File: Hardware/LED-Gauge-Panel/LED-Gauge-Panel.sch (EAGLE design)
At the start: 3 parts

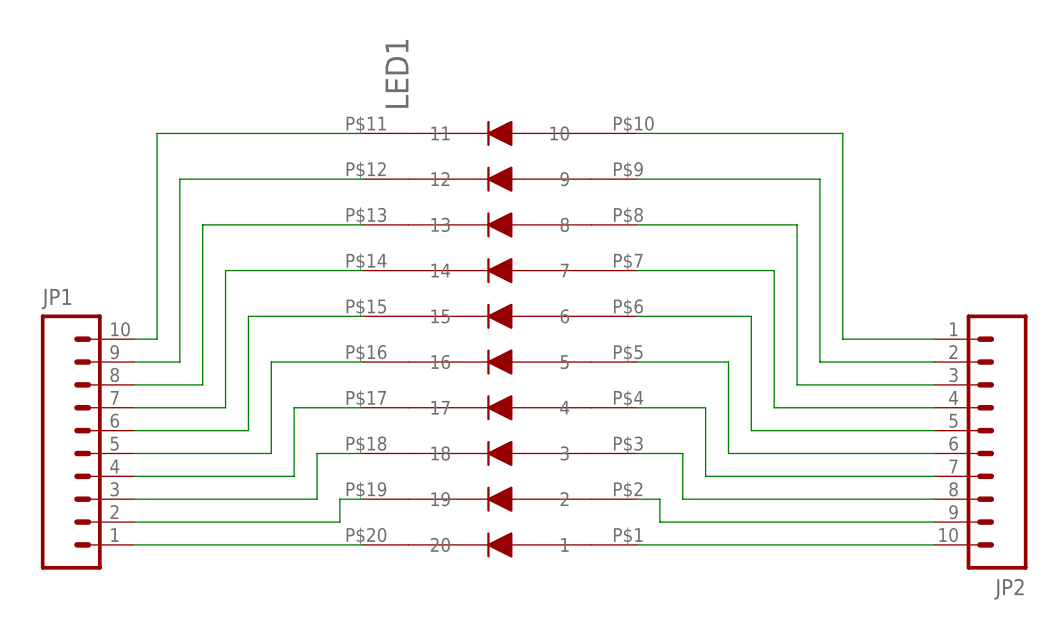
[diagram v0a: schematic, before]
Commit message: Create library part for LED display button, update PCB with LED button part
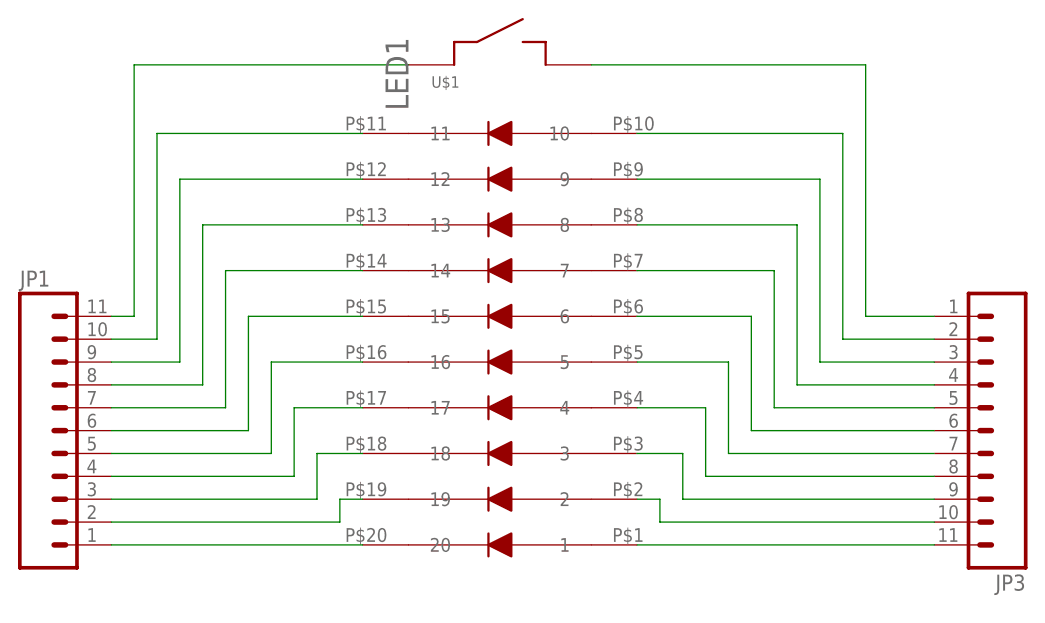
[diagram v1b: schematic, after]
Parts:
- removed JP2: (no value), SparkFun-Connectors:M10SILK_FEMALE_PTH
- added JP3: (no value), SparkFun-Connectors:M11PTH
- added U$1: MOMENTARY-SWITCH-EVQ1, 2016PowerPackLibraries:MOMENTARY-SWITCH-EVQ1
- JP1: device SparkFun-Connectors:M10SILK_FEMALE_PTH -> SparkFun-Connectors:M11PTH
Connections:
- new net N$21: JP1.11, U$1.P$1
- new net N$22: JP3.1, U$1.P$2
- net N$11: now also JP3.11; no longer JP2.10
- net N$12: now also JP3.10; no longer JP2.9
- net N$13: now also JP3.9; no longer JP2.8
- net N$14: now also JP3.8; no longer JP2.7
- net N$15: now also JP3.7; no longer JP2.6
- net N$16: now also JP3.6; no longer JP2.5
- net N$17: now also JP3.5; no longer JP2.4
- net N$18: now also JP3.4; no longer JP2.3
- net N$19: now also JP3.3; no longer JP2.2
- net N$20: now also JP3.2; no longer JP2.1
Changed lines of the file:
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@@
 <setting verticaltext="up"/>
 </settings>
-<grid distance="0.1" unitdist="inch" unit="inch" style="lines" multiple="1" display="yes" altdistance="0.01" altunitdist="inch" altunit="inch"/>
+<grid distance="0.1" unitdist="inch" unit="inch" style="lines" multiple="1" display="no" altdistance="0.01" altunitdist="inch" altunit="inch"/>
 <layers>
 <layer number="1" name="Top" color="4" fill="1" visible="no" active="no"/>
@@
 </classes>
 <parts>
-<part name="JP1" library="SparkFun-Connectors" deviceset="M10" device="SILK_FEMALE_PTH"/>
-<part name="JP2" library="SparkFun-Connectors" deviceset="M10" device="SILK_FEMALE_PTH"/>
+<part name="JP1" library="SparkFun-Connectors" deviceset="M11" device="PTH"/>
 <part name="LED1" library="2016PowerPackLibraries" deviceset="LED-DC7G3HWA" device=""/>
+<part name="U$1" library="2016PowerPackLibraries" deviceset="MOMENTARY-SWITCH-EVQ1" device=""/>
+<part name="JP3" library="SparkFun-Connectors" deviceset="M11" device="PTH"/>
 </parts>
 <sheets>
@@
 </plain>
 <instances>
-<instance part="JP1" gate="G$1" x="0" y="20.32"/>
-<instance part="JP2" gate="G$1" x="109.22" y="7.62" rot="R180"/>
+<instance part="JP1" gate="G$1" x="-2.54" y="15.24"/>
 <instance part="LED1" gate="G$1" x="55.88" y="2.54" rot="R90"/>
+<instance part="U$1" gate="G$1" x="45.72" y="55.88"/>
+<instance part="JP3" gate="G$1" x="109.22" y="15.24" rot="R180"/>
 </instances>
 <busses>
@@
 <pinref part="LED1" gate="G$1" pin="20"/>
 <pinref part="JP1" gate="G$1" pin="1"/>
-<wire x1="35.56" y1="2.54" x2="10.16" y2="2.54" width="0.1524" layer="91"/>
+<wire x1="35.56" y1="2.54" x2="7.62" y2="2.54" width="0.1524" layer="91"/>
 </segment>
 </net>
@@
 <wire x1="33.02" y1="7.62" x2="33.02" y2="5.08" width="0.1524" layer="91"/>
 <pinref part="JP1" gate="G$1" pin="2"/>
-<wire x1="33.02" y1="5.08" x2="10.16" y2="5.08" width="0.1524" layer="91"/>
+<wire x1="33.02" y1="5.08" x2="7.62" y2="5.08" width="0.1524" layer="91"/>
 </segment>
 </net>
@@
 <wire x1="30.48" y1="12.7" x2="30.48" y2="7.62" width="0.1524" layer="91"/>
 <pinref part="JP1" gate="G$1" pin="3"/>
-<wire x1="30.48" y1="7.62" x2="10.16" y2="7.62" width="0.1524" layer="91"/>
+<wire x1="30.48" y1="7.62" x2="7.62" y2="7.62" width="0.1524" layer="91"/>
 </segment>
 </net>
@@
 <wire x1="27.94" y1="17.78" x2="27.94" y2="10.16" width="0.1524" layer="91"/>
 <pinref part="JP1" gate="G$1" pin="4"/>
-<wire x1="27.94" y1="10.16" x2="10.16" y2="10.16" width="0.1524" layer="91"/>
+<wire x1="27.94" y1="10.16" x2="7.62" y2="10.16" width="0.1524" layer="91"/>
 </segment>
 </net>
@@
 <wire x1="25.4" y1="22.86" x2="25.4" y2="12.7" width="0.1524" layer="91"/>
 <pinref part="JP1" gate="G$1" pin="5"/>
-<wire x1="25.4" y1="12.7" x2="10.16" y2="12.7" width="0.1524" layer="91"/>
+<wire x1="25.4" y1="12.7" x2="7.62" y2="12.7" width="0.1524" layer="91"/>
 </segment>
 </net>
@@
 <wire x1="22.86" y1="27.94" x2="22.86" y2="15.24" width="0.1524" layer="91"/>
 <pinref part="JP1" gate="G$1" pin="6"/>
-<wire x1="22.86" y1="15.24" x2="10.16" y2="15.24" width="0.1524" layer="91"/>
+<wire x1="22.86" y1="15.24" x2="7.62" y2="15.24" width="0.1524" layer="91"/>
 </segment>
 </net>
@@
 <wire x1="20.32" y1="33.02" x2="20.32" y2="17.78" width="0.1524" layer="91"/>
 <pinref part="JP1" gate="G$1" pin="7"/>
-<wire x1="20.32" y1="17.78" x2="10.16" y2="17.78" width="0.1524" layer="91"/>
+<wire x1="20.32" y1="17.78" x2="7.62" y2="17.78" width="0.1524" layer="91"/>
 </segment>
 </net>
@@
 <wire x1="17.78" y1="38.1" x2="17.78" y2="20.32" width="0.1524" layer="91"/>
 <pinref part="JP1" gate="G$1" pin="8"/>
-<wire x1="17.78" y1="20.32" x2="10.16" y2="20.32" width="0.1524" layer="91"/>
+<wire x1="17.78" y1="20.32" x2="7.62" y2="20.32" width="0.1524" layer="91"/>
 </segment>
 </net>
@@
 <wire x1="15.24" y1="43.18" x2="15.24" y2="22.86" width="0.1524" layer="91"/>
 <pinref part="JP1" gate="G$1" pin="9"/>
-<wire x1="15.24" y1="22.86" x2="10.16" y2="22.86" width="0.1524" layer="91"/>
+<wire x1="15.24" y1="22.86" x2="7.62" y2="22.86" width="0.1524" layer="91"/>
 </segment>
 </net>
@@
 <segment>
 <pinref part="JP1" gate="G$1" pin="10"/>
-<wire x1="10.16" y1="25.4" x2="12.7" y2="25.4" width="0.1524" layer="91"/>
+<wire x1="7.62" y1="25.4" x2="12.7" y2="25.4" width="0.1524" layer="91"/>
 <wire x1="12.7" y1="25.4" x2="12.7" y2="48.26" width="0.1524" layer="91"/>
 <pinref part="LED1" gate="G$1" pin="11"/>
@@
 <segment>
 <pinref part="LED1" gate="G$1" pin="1"/>
-<pinref part="JP2" gate="G$1" pin="10"/>
 <wire x1="66.04" y1="2.54" x2="99.06" y2="2.54" width="0.1524" layer="91"/>
+<pinref part="JP3" gate="G$1" pin="11"/>
 </segment>
 </net>
 <net name="N$12" class="0">
 <segment>
-<pinref part="JP2" gate="G$1" pin="9"/>
 <wire x1="99.06" y1="5.08" x2="68.58" y2="5.08" width="0.1524" layer="91"/>
 <wire x1="68.58" y1="5.08" x2="68.58" y2="7.62" width="0.1524" layer="91"/>
 <pinref part="LED1" gate="G$1" pin="2"/>
 <wire x1="68.58" y1="7.62" x2="66.04" y2="7.62" width="0.1524" layer="91"/>
+<pinref part="JP3" gate="G$1" pin="10"/>
 </segment>
 </net>
 <net name="N$13" class="0">
 <segment>
-<pinref part="JP2" gate="G$1" pin="8"/>
 <wire x1="99.06" y1="7.62" x2="71.12" y2="7.62" width="0.1524" layer="91"/>
 <wire x1="71.12" y1="7.62" x2="71.12" y2="12.7" width="0.1524" layer="91"/>
 <pinref part="LED1" gate="G$1" pin="3"/>
 <wire x1="71.12" y1="12.7" x2="66.04" y2="12.7" width="0.1524" layer="91"/>
+<pinref part="JP3" gate="G$1" pin="9"/>
 </segment>
 </net>
 <net name="N$14" class="0">
 <segment>
-<pinref part="JP2" gate="G$1" pin="7"/>
 <wire x1="99.06" y1="10.16" x2="73.66" y2="10.16" width="0.1524" layer="91"/>
 <wire x1="73.66" y1="10.16" x2="73.66" y2="17.78" width="0.1524" layer="91"/>
 <pinref part="LED1" gate="G$1" pin="4"/>
 <wire x1="73.66" y1="17.78" x2="66.04" y2="17.78" width="0.1524" layer="91"/>
+<pinref part="JP3" gate="G$1" pin="8"/>
 </segment>
 </net>
 <net name="N$15" class="0">
 <segment>
-<pinref part="JP2" gate="G$1" pin="6"/>
 <wire x1="99.06" y1="12.7" x2="76.2" y2="12.7" width="0.1524" layer="91"/>
 <wire x1="76.2" y1="12.7" x2="76.2" y2="22.86" width="0.1524" layer="91"/>
 <pinref part="LED1" gate="G$1" pin="5"/>
 <wire x1="76.2" y1="22.86" x2="66.04" y2="22.86" width="0.1524" layer="91"/>
+<pinref part="JP3" gate="G$1" pin="7"/>
 </segment>
 </net>
 <net name="N$16" class="0">
 <segment>
-<pinref part="JP2" gate="G$1" pin="5"/>
 <wire x1="99.06" y1="15.24" x2="78.74" y2="15.24" width="0.1524" layer="91"/>
 <wire x1="78.74" y1="15.24" x2="78.74" y2="27.94" width="0.1524" layer="91"/>
 <pinref part="LED1" gate="G$1" pin="6"/>
 <wire x1="78.74" y1="27.94" x2="66.04" y2="27.94" width="0.1524" layer="91"/>
+<pinref part="JP3" gate="G$1" pin="6"/>
 </segment>
 </net>
 <net name="N$17" class="0">
 <segment>
-<pinref part="JP2" gate="G$1" pin="4"/>
 <wire x1="99.06" y1="17.78" x2="81.28" y2="17.78" width="0.1524" layer="91"/>
 <wire x1="81.28" y1="17.78" x2="81.28" y2="33.02" width="0.1524" layer="91"/>
 <pinref part="LED1" gate="G$1" pin="7"/>
 <wire x1="81.28" y1="33.02" x2="66.04" y2="33.02" width="0.1524" layer="91"/>
+<pinref part="JP3" gate="G$1" pin="5"/>
 </segment>
 </net>
 <net name="N$18" class="0">
 <segment>
-<pinref part="JP2" gate="G$1" pin="3"/>
 <wire x1="99.06" y1="20.32" x2="83.82" y2="20.32" width="0.1524" layer="91"/>
 <wire x1="83.82" y1="20.32" x2="83.82" y2="38.1" width="0.1524" layer="91"/>
 <pinref part="LED1" gate="G$1" pin="8"/>
 <wire x1="83.82" y1="38.1" x2="66.04" y2="38.1" width="0.1524" layer="91"/>
+<pinref part="JP3" gate="G$1" pin="4"/>
 </segment>
 </net>
 <net name="N$19" class="0">
 <segment>
-<pinref part="JP2" gate="G$1" pin="2"/>
 <wire x1="99.06" y1="22.86" x2="86.36" y2="22.86" width="0.1524" layer="91"/>
 <wire x1="86.36" y1="22.86" x2="86.36" y2="43.18" width="0.1524" layer="91"/>
 <pinref part="LED1" gate="G$1" pin="9"/>
 <wire x1="86.36" y1="43.18" x2="66.04" y2="43.18" width="0.1524" layer="91"/>
+<pinref part="JP3" gate="G$1" pin="3"/>
 </segment>
 </net>
 <net name="N$20" class="0">
 <segment>
-<pinref part="JP2" gate="G$1" pin="1"/>
 <wire x1="99.06" y1="25.4" x2="88.9" y2="25.4" width="0.1524" layer="91"/>
 <wire x1="88.9" y1="25.4" x2="88.9" y2="48.26" width="0.1524" layer="91"/>
 <pinref part="LED1" gate="G$1" pin="10"/>
 <wire x1="88.9" y1="48.26" x2="66.04" y2="48.26" width="0.1524" layer="91"/>
-</segment>
-</net>
+<pinref part="JP3" gate="G$1" pin="2"/>
+</segment>
+</net>
+<net name="N$21" class="0">
+<segment>
+<pinref part="JP1" gate="G$1" pin="11"/>
+<wire x1="7.62" y1="27.94" x2="10.16" y2="27.94" width="0.1524" layer="91"/>
+<wire x1="10.16" y1="27.94" x2="10.16" y2="55.88" width="0.1524" layer="91"/>
+<pinref part="U$1" gate="G$1" pin="P$1"/>
+<wire x1="10.16" y1="55.88" x2="40.64" y2="55.88" width="0.1524" layer="91"/>
+</segment>
+</net>
+<net name="N$22" class="0">
+<segment>
+<pinref part="U$1" gate="G$1" pin="P$2"/>
+<wire x1="60.96" y1="55.88" x2="91.44" y2="55.88" width="0.1524" layer="91"/>
+<wire x1="91.44" y1="55.88" x2="91.44" y2="27.94" width="0.1524" layer="91"/>
+<pinref part="JP3" gate="G$1" pin="1"/>
+<wire x1="91.44" y1="27.94" x2="99.06" y2="27.94" width="0.1524" layer="91"/>
+</segment>
+</net>
